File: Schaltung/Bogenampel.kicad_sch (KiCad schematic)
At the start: 31 parts, among them J1 Input 1, J10 Display, J2 Input 2, J3 Input 3, J4 Input 4, J5 Input 5, J6 Power Bank, J7 Battery, J8 KY-006, J9 WS2812B Stripe Timer, U1 NRF24L01_Breakout, U2 TXS0108EPW

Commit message: Fix: NRF24L01 Funkverbindung - Konfiguration korrigiert
Mehrere kritische Probleme behoben:

1. Payload-Größe synchronisiert
   - Sender: 4 Bytes → 2 Bytes (passend zu RadioPacket)
   - Empfänger: bereits korrekt 2 Bytes

2. Pin-Initialisierung korrigiert
   - Entfernt manuelle CE/CSN Pin-Init (RF24.begin() macht das)
   - Verhindert Konflikte mit RF24-Bibliothek

3. SPI-Bus-Initialisierung optimiert (Sender)
   - SPI.begin() einmal am Anfang von setup()
   - Radio VOR Display initialisieren (verhindert SPI-Konflikte)
   - Doppelte SPI.begin() Aufrufe entfernt

4. RF24-Enums direkt verwendet
   - Entfernt custom DataRate/PowerLevel Enums
   - Verwendet rf24_datarate_e und rf24_pa_dbm_e direkt
   - Behebt Type-Cast Probleme

5. Namenskonflikte behoben
   - Groups::Type::CD → Groups::Type::GROUP_CD
   - Konflikt mit RF24 Makro #define CD 0x09

6. Debug-Ausgaben erweitert
   - Manuelle Radio-Diagnose hinzugefügt
   - isChipConnected(), getChannel(), etc.

Hardware-Problem identifiziert:
- NRF24L01 benötigt 3.3V (nicht 5V!)
- Kondensator 10-100µF empfohlen
- Evtl. Level-Shifter für 5V↔3.3V Logik nötig

🤖 Generated with [Claude Code](https://claude.com/claude-code)

Co-Authored-By: Claude Sonnet 4.5 <noreply@anthropic.com>
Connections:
- net SPI.MISO: now also A2.15 (D12), U1.7 (MISO); no longer A2.14 (D11), U1.6 (MOSI)
- net SPI.MOSI: now also A2.14 (D11), U1.6 (MOSI); no longer A2.15 (D12), U1.7 (MISO)
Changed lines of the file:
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@@
+	)
+	(bus_entry
+		(at 82.55 124.46)
+		(size 2.54 -2.54)
+		(stroke
+			(width 0)
+			(type default)
+		)
+	)
+	(bus_entry
+		(at 82.55 129.54)
+		(size 2.54 -2.54)
+		(stroke
+			(width 0)
+			(type default)
+		)
+	)
+	(bus_entry
+		(at 71.12 121.92)
+		(size -2.54 2.54)
+		(stroke
+			(width 0)
+			(type default)
+		)
+	)
+	(bus_entry
+		(at 191.77 139.7)
+		(size 2.54 -2.54)
+		(stroke
+			(width 0)
+			(type default)
+		)
 	)
 	(bus_entry
@@
 	)
 	(bus_entry
-		(at 82.55 129.54)
-		(size 2.54 -2.54)
-		(stroke
-			(width 0)
-			(type default)
-		)
-	)
-	(bus_entry
-		(at 191.77 139.7)
-		(size 2.54 -2.54)
-		(stroke
-			(width 0)
-			(type default)
-		)
-	)
-	(bus_entry
-		(at 82.55 124.46)
-		(size 2.54 -2.54)
-		(stroke
-			(width 0)
-			(type default)
-		)
-	)
-	(bus_entry
 		(at 191.77 144.78)
 		(size 2.54 -2.54)
@@
 		)
 	)
-	(bus_entry
-		(at 71.12 121.92)
-		(size -2.54 2.54)
-		(stroke
-			(width 0)
-			(type default)
-		)
-	)
 	(wire
 		(pts
@@
 	(bus
 		(pts
+			(xy 82.55 127) (xy 82.55 129.54)
+		)
+		(stroke
+			(width 0)
+			(type default)
+		)
+	)
+	(bus
+		(pts
 			(xy 82.55 157.48) (xy 71.12 157.48)
 		)
@@
 		)
 	)
+	(bus
+		(pts
+			(xy 71.12 121.92) (xy 71.12 124.46)
+		)
+		(stroke
+			(width 0)
+			(type default)
+		)
+	)
 	(wire
 		(pts
@@
 		)
 	)
+	(wire
+		(pts
+			(xy 176.53 93.98) (xy 176.53 95.25)
+		)
+		(stroke
+			(width 0)
+			(type default)
+		)
+	)
+	(wire
+		(pts
+			(xy 241.3 139.7) (xy 241.3 144.78)
+		)
+		(stroke
+			(width 0)
+			(type default)
+		)
+	)
+	(wire
+		(pts
+			(xy 176.53 102.87) (xy 176.53 104.14)
+		)
+		(stroke
+			(width 0)
+			(type default)
+		)
+	)
+	(wire
+		(pts
+			(xy 107.95 137.16) (xy 110.49 137.16)
+		)
+		(stroke
+			(width 0)
+			(type default)
+		)
+	)
+	(wire
+		(pts
+			(xy 194.31 137.16) (xy 208.28 137.16)
+		)
+		(stroke
+			(width 0)
+			(type default)
+		)
+	)
+	(wire
+		(pts
+			(xy 128.27 43.18) (xy 128.27 68.58)
+		)
+		(stroke
+			(width 0)
+			(type default)
+		)
+	)
+	(wire
+		(pts
+			(xy 161.29 90.17) (xy 161.29 124.46)
+		)
+		(stroke
+			(width 0)
+			(type default)
+		)
+	)
 	(bus
 		(pts
@@
 	(wire
 		(pts
-			(xy 176.53 93.98) (xy 176.53 95.25)
-		)
-		(stroke
-			(width 0)
-			(type default)
-		)
-	)
-	(wire
-		(pts
-			(xy 241.3 139.7) (xy 241.3 144.78)
-		)
-		(stroke
-			(width 0)
-			(type default)
-		)
-	)
-	(wire
-		(pts
-			(xy 176.53 102.87) (xy 176.53 104.14)
-		)
-		(stroke
-			(width 0)
-			(type default)
-		)
-	)
-	(wire
-		(pts
-			(xy 107.95 137.16) (xy 110.49 137.16)
-		)
-		(stroke
-			(width 0)
-			(type default)
-		)
-	)
-	(wire
-		(pts
-			(xy 194.31 137.16) (xy 208.28 137.16)
-		)
-		(stroke
-			(width 0)
-			(type default)
-		)
-	)
-	(wire
-		(pts
-			(xy 128.27 43.18) (xy 128.27 68.58)
-		)
-		(stroke
-			(width 0)
-			(type default)
-		)
-	)
-	(wire
-		(pts
-			(xy 161.29 90.17) (xy 161.29 124.46)
-		)
-		(stroke
-			(width 0)
-			(type default)
-		)
-	)
-	(bus
-		(pts
-			(xy 71.12 121.92) (xy 71.12 124.46)
-		)
-		(stroke
-			(width 0)
-			(type default)
-		)
-	)
-	(wire
-		(pts
 			(xy 127 111.76) (xy 127 132.08)
 		)
@@
 		(pts
 			(xy 138.43 119.38) (xy 120.65 119.38)
-		)
-		(stroke
-			(width 0)
-			(type default)
-		)
-	)
-	(bus
-		(pts
-			(xy 82.55 127) (xy 82.55 129.54)
 		)
 		(stroke
@@
 		)
 	)
-	(label "SPI.MOSI"
-		(at 58.42 124.46 0)
-		(effects
-			(font
-				(size 1.27 1.27)
-			)
-			(justify left bottom)
-		)
-	)
 	(label "SPI.SCK"
 		(at 194.31 137.16 0)
@@
 		)
 	)
-	(label "SPI.MISO"
-		(at 58.42 121.92 0)
-		(effects
-			(font
-				(size 1.27 1.27)
-			)
-			(justify left bottom)
-		)
-	)
 	(label "SPI.MOSI"
 		(at 194.31 134.62 0)
@@
 		)
 	)
-	(label "SPI.MOSI"
-		(at 85.09 124.46 0)
-		(effects
-			(font
-				(size 1.27 1.27)
-			)
-			(justify left bottom)
-		)
-	)
 	(label "UI_CS"
 		(at 194.31 127 0)
@@
 	)
 	(label "SPI.MISO"
-		(at 85.09 121.92 0)
+		(at 85.09 124.46 0)
+		(effects
+			(font
+				(size 1.27 1.27)
+			)
+			(justify left bottom)
+		)
+	)
+	(label "SPI.MISO"
+		(at 58.42 124.46 0)
+		(effects
+			(font
+				(size 1.27 1.27)
+			)
+			(justify left bottom)
+		)
+	)
+	(label "SPI.MOSI"
+		(at 58.42 121.92 0)
 		(effects
 			(font
@@
 		(effects
 			(font
+				(size 1.27 1.27)
+			)
+			(justify left bottom)
+		)
+	)
+	(label "SPI.MOSI"
+		(at 85.09 121.92 0)
+		(effects
+			(font

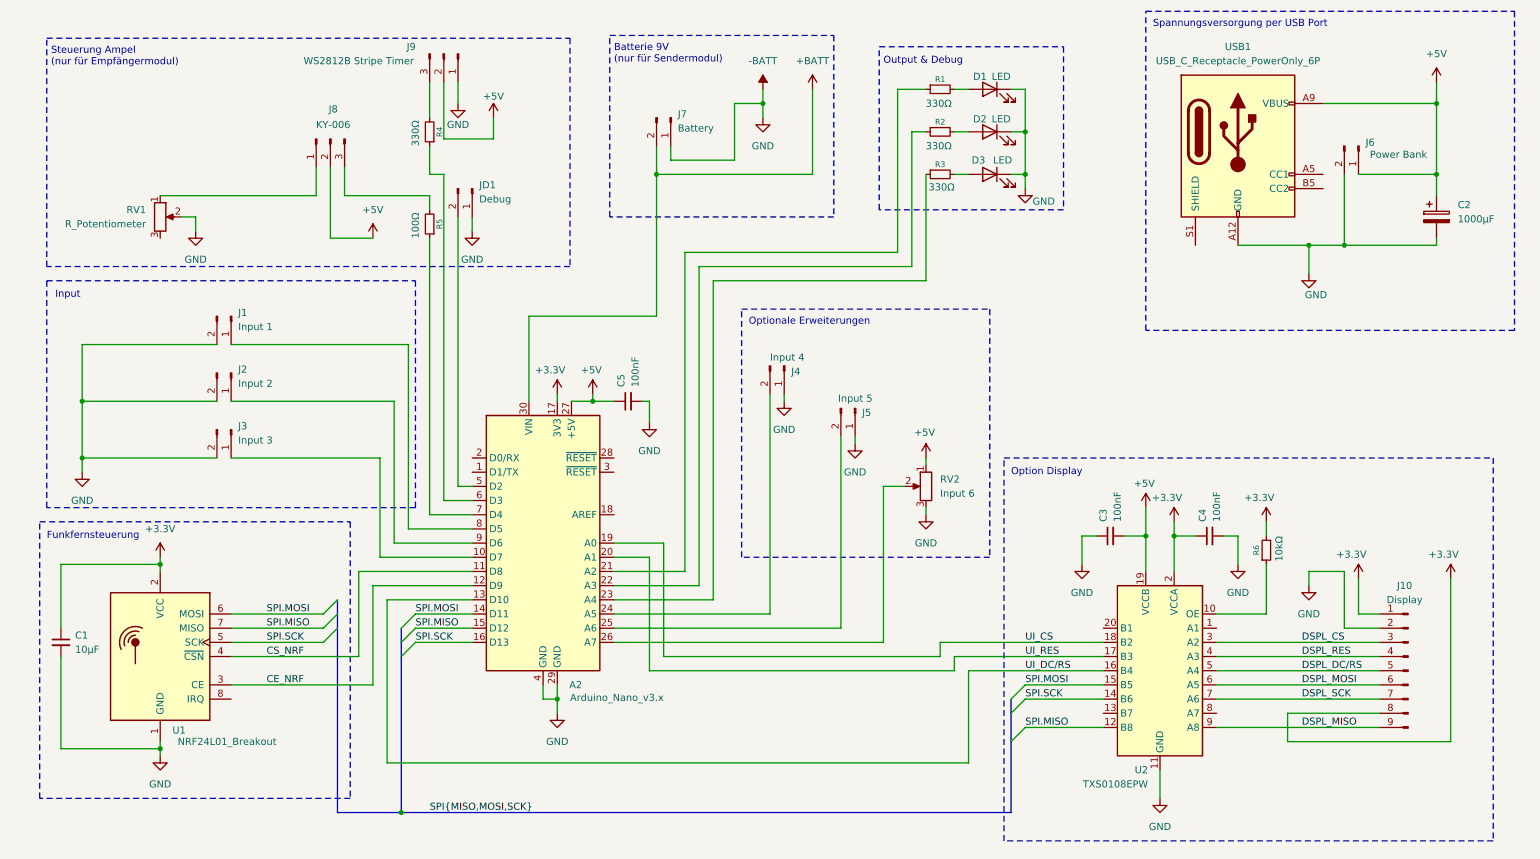
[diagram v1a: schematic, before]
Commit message: UI-Verbesserungen und Funk-Debugging
Schießbetrieb UI:
- Überschrift in Orange mit Trennlinie
- Timer horizontal zentriert und nur 1x pro Sekunde aktualisiert
- Layout-Abstände optimiert (weniger gestaucht)
- Button "Passe beenden" mit grauem Hintergrund
- Bei 3-4 Schützen: Timer tiefer positioniert

Gruppenanzeige:
- Vereinheitlichtes Format für PfeileHolenMenu und Schießbetrieb
- Statischer String "{A/B -> C/D} {C/D -> A/B}"
- Aktuelle Gruppe gelb hervorgehoben, Rest grau
- "Nächste:" in PfeileHolenMenu, "Aktuell:" in Schießbetrieb

Funk-Debugging:
- Kontinuierliche PING-Tests im Splash Screen (alle 2 Sek)
- Pipe-Adresse wird beim Start ausgegeben
- Versucht printDetails() mit Serial.flush()
- Empfänger auf Pipe 1 umgestellt (statt Pipe 0)

🤖 Generated with [Claude Code](https://claude.com/claude-code)

Co-Authored-By: Claude Sonnet 4.5 <noreply@anthropic.com>
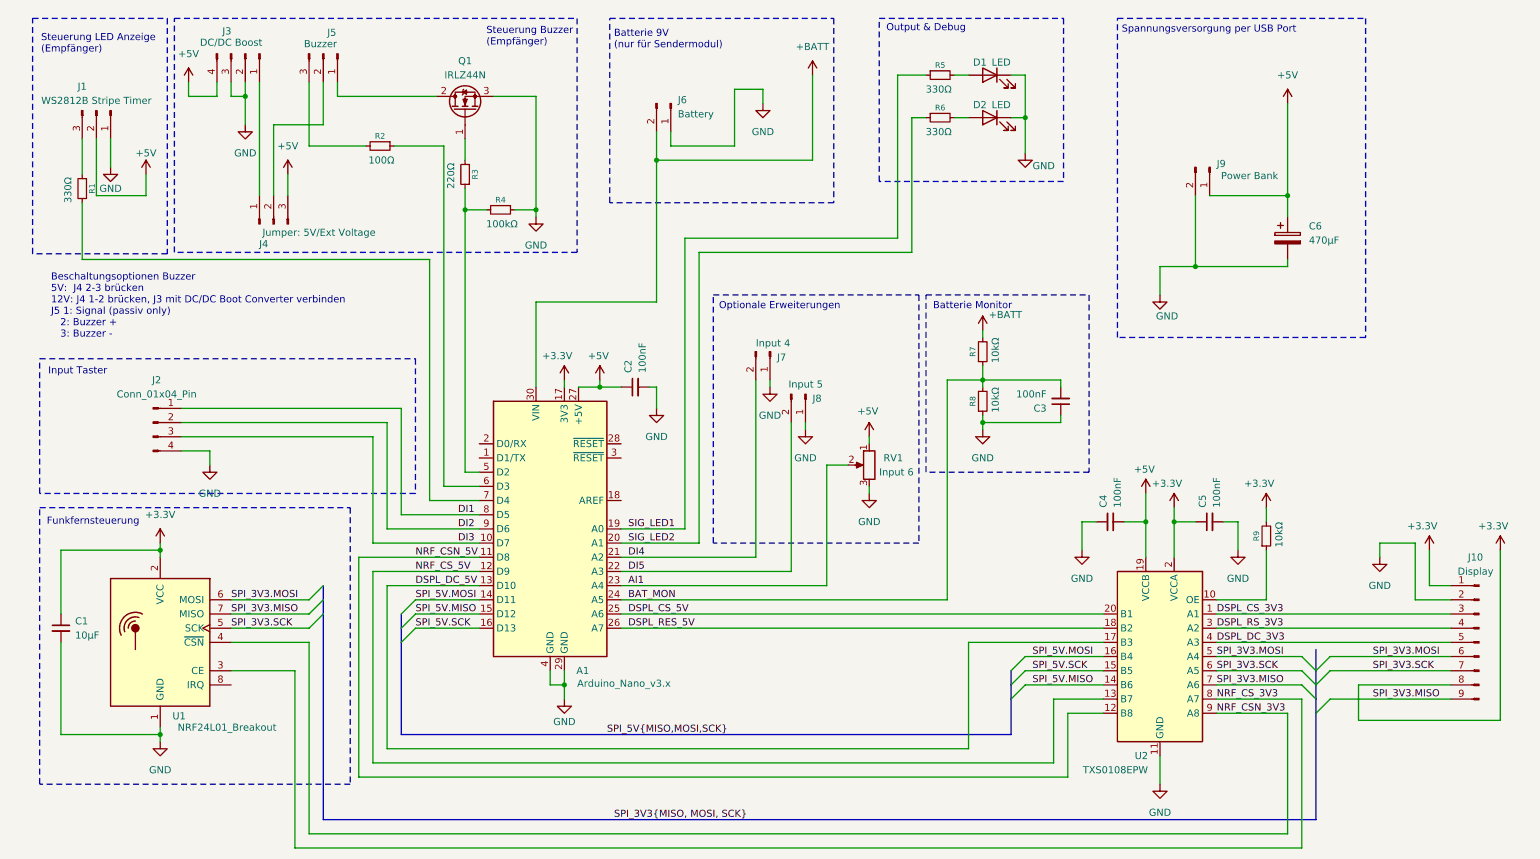
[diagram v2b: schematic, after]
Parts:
- removed D3: LED, LED_THT:LED_D3.0mm, symbol Device:LED
- removed J1: Input 1, Connector_JST:JST_XH_B2B-XH-A_1x02_P2.50mm_Vertical, symbol Connector:Conn_01x02_Pin
- removed J2: Input 2, Connector_JST:JST_XH_B2B-XH-A_1x02_P2.50mm_Vertical, symbol Connector:Conn_01x02_Pin
- removed J3: Input 3, Connector_JST:JST_XH_B2B-XH-A_1x02_P2.50mm_Vertical, symbol Connector:Conn_01x02_Pin
- removed JD1: Debug, Connector_PinHeader_2.54mm:PinHeader_1x02_P2.54mm_Vertical, symbol Connector:Conn_01x02_Pin
- removed R3: 330Ω, Resistor_SMD:R_1206_3216Metric, symbol Device:R_Small
- removed RV1: R_Potentiometer, Connector_JST:JST_XH_B3B-XH-A_1x03_P2.50mm_Vertical, symbol Device:R_Potentiometer
- removed USB1: USB_C_Receptacle_PowerOnly_6P, symbol Connector:USB_C_Receptacle_PowerOnly_6P
- added C3: 100nF, Capacitor_SMD:C_1206_3216Metric, symbol Device:C_Small
- added J2: Conn_01x04_Pin, Connector_JST:JST_XH_B4B-XH-A_1x04_P2.50mm_Vertical, symbol Connector:Conn_01x04_Pin
- added J3: DC/DC Boost, Connector_JST:JST_XH_B4B-XH-A_1x04_P2.50mm_Vertical, symbol Connector:Conn_01x04_Pin
- added J4: Jumper: 5V/Ext Voltage, Connector_PinHeader_2.54mm:PinHeader_1x03_P2.54mm_Vertical, symbol Connector:Conn_01x03_Pin
- added Q1: IRLZ44N, Package_TO_SOT_THT:TO-220-3_Vertical, symbol Transistor_FET:IRLZ44N
- added R2: 100Ω, Resistor_SMD:R_1206_3216Metric, symbol Device:R_Small
- added R4: 100kΩ, Resistor_SMD:R_1206_3216Metric, symbol Device:R_Small
- added R7, R8: 10kΩ, Resistor_SMD:R_1206_3216Metric, symbol Device:R_Small
- C6: renamed from C2; value 1000µF -> 470µF
- J5: renamed from J8; value KY-006 -> Buzzer
- R3: renamed from R5; value 100Ω -> 220Ω
- renumbered A2 to A1, C5 to C2, C3 to C4, C4 to C5, J9 to J1, J7 to J6, J4 to J7, J5 to J8, J6 to J9, R4 to R1, R1 to R5, R2 to R6, R6 to R9, RV2 to RV1
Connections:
- net +5V: now also J3.4 (Pin_4), J4.3 (Pin_3); no longer J5.2 (Pin_2)
- net +BATT: now also R7.2
- net DI4: now reaches A1.21 (A2)
- net DI4: now also J7.2 (Pin_2); no longer R5.1
- net AI1: now reaches RV1.2
- net AI1: now also A1.23 (A4); no longer A1.26 (A7)
- net at J5.1 (Pin_1): now also Q1.2 (D)
- net DI5: now reaches A1.22 (A3)
- net DI5: now also J8.2 (Pin_2); no longer R6.1
- net BAT_MON: now reaches A1.24 (A5)
- net BAT_MON: now also C3.2, R7.1, R8.2; no longer J7.2 (Pin_2)
- net DI3: now reaches A1.10 (D7)
- net DI3: now also J2.3 (Pin_3)
- net at R3.1: now also A1.5 (D2), R4.2; no longer A1.7 (D4)
- net at R3.2: now also Q1.1 (G); no longer J5.3 (Pin_3)
- net DI1: now reaches A1.8 (D5)
- net DI1: now also J2.1 (Pin_1)
- net DSPL_CS_5V: now reaches A1.25 (A6)
- net DSPL_CS_5V: now also U2.20 (B1); no longer J8.2 (Pin_2)
- net DSPL_RES_5V: now reaches U2.18 (B2)
- net DSPL_RES_5V: now also A1.26 (A7); no longer A1.19 (A0)
- net at A1.6 (D3): now also R2.1; no longer R1.1
- net DI2: now reaches A1.9 (D6)
- net DI2: now also J2.2 (Pin_2)
- net DSPL_CS_3V3: now reaches U2.1 (A1)
- net DSPL_CS_3V3: now also J10.3 (Pin_3)
- net NRF_CS_5V: now reaches U2.13 (B7)
- net NRF_CS_5V: now also A1.12 (D9)
- net NRF_CS_3V3: now reaches U2.8 (A7)
- net NRF_CS_3V3: now also U1.3 (CE)
- net -BATT renamed GND
- net GND: now also C3.1, J2.4 (Pin_4), J3.2 (Pin_2), J3.3 (Pin_3), Q1.3 (S), R4.1, R8.1
- removed net CE_NRF: A1.12 (D9), U1.3 (CE)
- net CS_NRF renamed NRF_CSN_3V3
- net NRF_CSN_3V3: now also U2.9 (A8); no longer A1.11 (D8)
- net DSPL_CS renamed DSPL_RS_3V3
- net DSPL_RS_3V3: now also J10.4 (Pin_4); no longer J10.3 (Pin_3)
- net DSPL_DC/RS renamed DSPL_DC_3V3
- net DSPL_DC_3V3: now also U2.4 (A3); no longer U2.5 (A4)
- net DSPL_MISO renamed SPI_3V3.MISO
- net SPI_3V3.MISO: now also U1.7 (MISO), U2.7 (A6); no longer U2.9 (A8)
- net DSPL_MOSI renamed SPI_3V3.MOSI
- net SPI_3V3.MOSI: now also U1.6 (MOSI), U2.5 (A4); no longer U2.6 (A5)
- removed net DSPL_RES: J10.4 (Pin_4), U2.4 (A3)
- net DSPL_SCK renamed SPI_3V3.SCK
- net SPI_3V3.SCK: now also U1.5 (SCK), U2.6 (A5); no longer U2.7 (A6)
- removed net SPI.MISO: A1.15 (D12), U1.7 (MISO), U2.12 (B8)
- removed net SPI.MOSI: A1.14 (D11), U1.6 (MOSI), U2.15 (B5)
- removed net SPI.SCK: A1.16 (D13), U1.5 (SCK), U2.14 (B6)
- net UI_DC/RS renamed DSPL_DC_5V
- net DSPL_DC_5V: now also U2.17 (B3); no longer U2.16 (B4)
- net UI_RES renamed SIG_LED2
- net SIG_LED2: now also R6.1; no longer U2.17 (B3)
- new net: J3.1 (Pin_1), J4.1 (Pin_1)
- new net: J4.2 (Pin_2), J5.2 (Pin_2)
- new net: J5.3 (Pin_3), R2.2
- new net: A1.7 (D4), R1.1
- new net NRF_CSN_5V: A1.11 (D8), U2.12 (B8)
- new net SIG_LED1: A1.19 (A0), R5.1
- new net SPI_5V.MISO: A1.15 (D12), U2.14 (B6)
- new net SPI_5V.MOSI: A1.14 (D11), U2.16 (B4)
- new net SPI_5V.SCK: A1.16 (D13), U2.15 (B5)
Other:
- note added: "Batterie Monitor"
- note added: "Beschaltungsoptionen Buzzer 5V: J4 2-3 brücken 12V: J4 1-2 brücken, J3 mit DC/DC Boot Converter verbinden J5 1: Signal (passiv only) 2: Buzzer + 3: Buzzer -"
- note added: "Input Taster"
- note added: "Steuerung Buzzer (Empfänger)"
- note added: "Steuerung LED Anzeige (Empfänger)"
- note removed: "Input"
- note removed: "Option Display"
- note removed: "Steuerung Ampel (nur für Empfängermodul)"
- moved on the sheet: A1, C1, C2, C4, C5, C6, D1, D2, J1, J10, J5, J6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

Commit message: 7-Segment LED-Display und Gruppen-Anzeige implementiert
Empfänger:
- 158 LEDs konfiguriert: 16 Gruppe A/B, 16 Gruppe C/D, 126 für 3×7-Segment Displays
- Timer-Countdown auf 7-Segment-Display (Grün > Orange > Rot)
- Vorbereitungsphase (10s) mit Countdown in ROT
- Orange statt Gelb für letzte 30 Sekunden (besserer Kontrast zu Grün)
- Gruppen-Farbe synchron mit Display-Farbe
- Gruppen-Umschaltung korrigiert (inaktive Gruppe wird ausgeschaltet)
- Buzzer-Funktionen verbessert (explizites Pin-Reset)
- segmentMap korrigiert für korrekte 7-Segment-Darstellung
- Display-Reihenfolge angepasst (1er, 10er, 100er von links nach rechts)

Sender:
- Gruppen-Kommandos jetzt zur richtigen Zeit gesendet (nach advanceToNextGroup)

🤖 Generated with Claude Code

Co-Authored-By: Claude Sonnet 4.5 <noreply@anthropic.com>
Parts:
- removed C1: 10µF, Capacitor_SMD:C_1206_3216Metric, symbol Device:C_Small
- added C1: 100µF, Capacitor_THT:CP_Radial_D8.0mm_P3.50mm, symbol Device:C_Polarized
- added C5: 100nF, Capacitor_SMD:C_1206_3216Metric, symbol Device:C_Small
- added C7, C8: 10µF, Capacitor_SMD:C_1206_3216Metric, symbol Device:C_Small
- added U3: LM1117DT-3.3, Package_TO_SOT_SMD:TO-252-3_TabPin2, symbol Regulator_Linear:LM1117DT-3.3
- renumbered C5 to C6, C6 to C9
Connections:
- net +3.3V: now also C1.1, C5.1, C7.1, U3.2 (VO); no longer A1.17 (3V3)
- net +5V: now also C8.1, U3.3 (VI)
- net GND: now also C1.2, C5.2, C7.2, C8.2, U3.1 (GND)
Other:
- moved on the sheet: C9, J9
